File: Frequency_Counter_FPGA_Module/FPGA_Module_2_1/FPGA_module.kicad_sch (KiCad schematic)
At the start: 0 parts

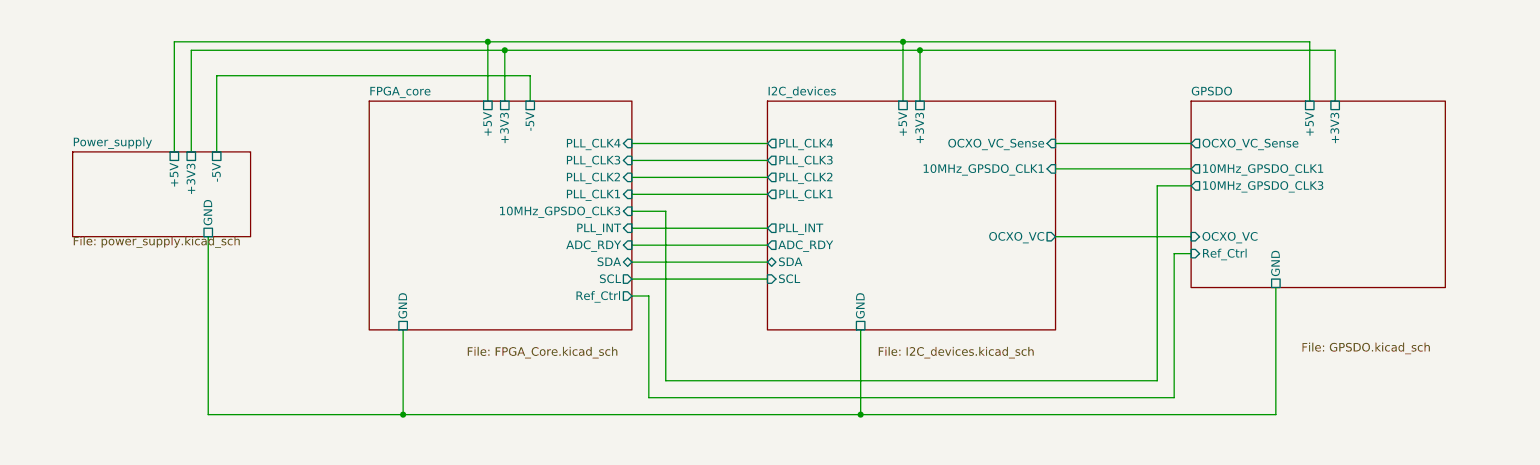
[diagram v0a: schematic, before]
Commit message: chore(hw): KiCad nosne desky FPGA 2.0 -> 2.1 (vc. Gerberu)
Zalohy KiCadu (FPGA_module-backups/, *-bak) ignoruje .gitignore.

Co-Authored-By: Claude Opus 5.5 <noreply@anthropic.com>
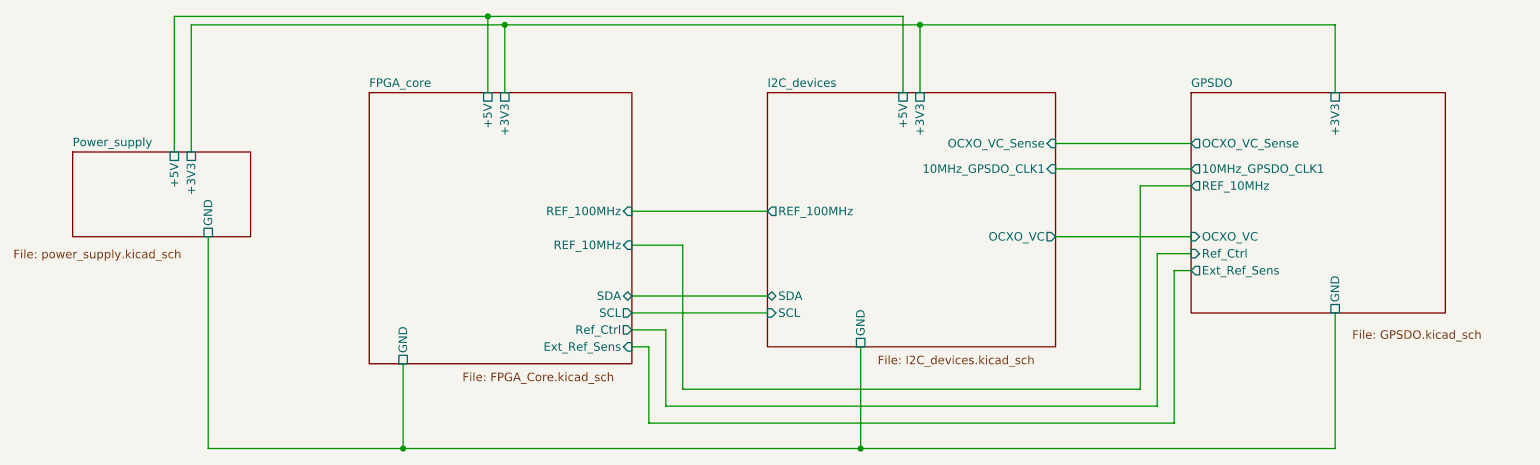
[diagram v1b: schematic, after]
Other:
- sheet FPGA_core ports: added Ext_Ref_Sens, REF_100MHz, REF_10MHz; removed -5V, 10MHz_GPSDO_CLK3, ADC_RDY, PLL_CLK1, PLL_CLK2, PLL_CLK3, PLL_CLK4, PLL_INT
- sheet GPSDO ports: added Ext_Ref_Sens, REF_10MHz; removed +5V, 10MHz_GPSDO_CLK3
- sheet I2C_devices ports: added REF_100MHz; removed ADC_RDY, PLL_CLK1, PLL_CLK2, PLL_CLK3, PLL_CLK4, PLL_INT
- sheet Power_supply ports: added none; removed -5V
